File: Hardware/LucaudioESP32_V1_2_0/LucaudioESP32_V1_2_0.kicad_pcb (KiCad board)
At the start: 2 copper layers, 92.4 x 70 mm, 93 parts, among them J1 Conn_01x04_Pin, J2 Conn_Coaxial_x2, J3 USB_C_Receptacle_USB2.0_16P, J4 Conn_01x04_Socket, J5 Conn_01x05_Socket, J6 Conn_01x05_Pin, J8 USB_B_Micro, J9 AudioJack3, Q1 BC847, Q2 BC847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

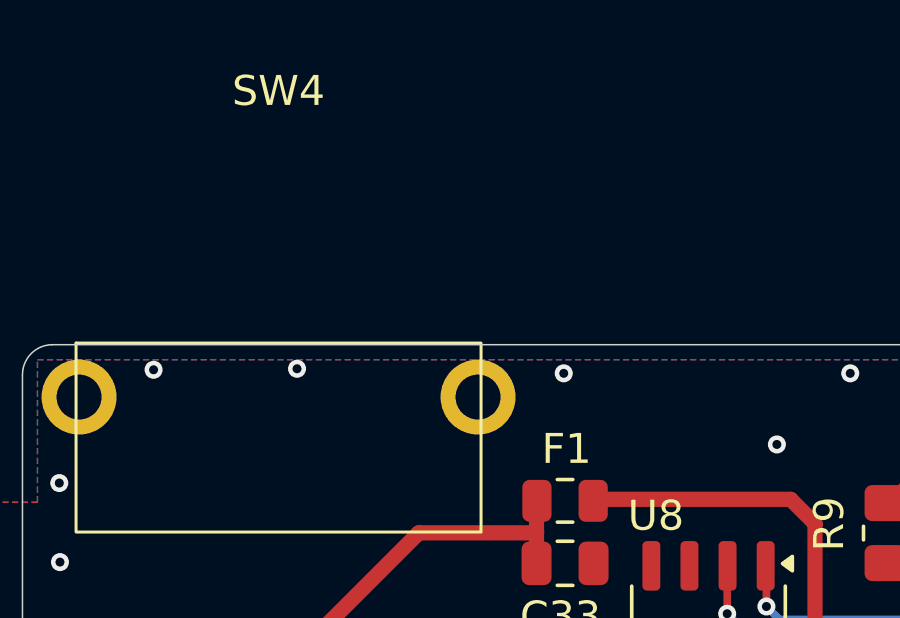
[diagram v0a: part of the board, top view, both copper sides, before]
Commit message: Revamping folders and added 2.0 and 2.1 on git
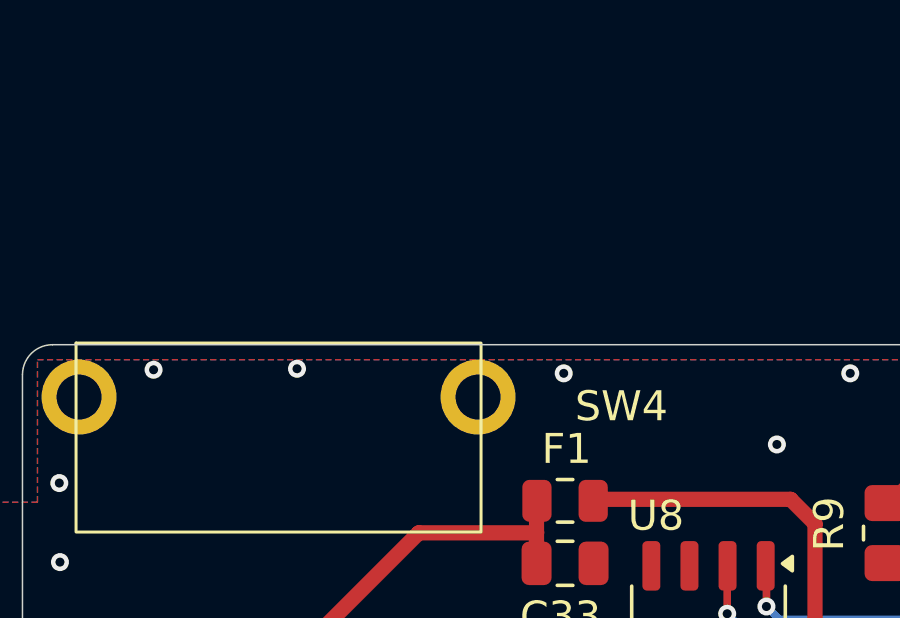
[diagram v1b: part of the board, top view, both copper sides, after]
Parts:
- Q1, Q2: value BC847 -> BC857
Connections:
- Q1 pad 2: Net-(Q1-E) -> 3V3_o
- Q1 pad 3: 3V3_o -> Net-(Q1-C)
- Q2 pad 2: Net-(Q2-E) -> 3V3_o
- Q2 pad 3: 3V3_o -> Net-(Q2-C)
- R10 pad 2: Net-(Q1-E) -> Net-(Q1-C)
- R13 pad 2: Net-(Q2-E) -> Net-(Q2-C)
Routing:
- net Net-(Q2-E): track 3.58 -> 0.00 mm
- net Net-(Q2-C): track 0.00 -> 3.58 mm
- net Net-(Q1-E): track 3.45 -> 0.00 mm
- net 3V3_o: track 64.7 -> 68.2 mm
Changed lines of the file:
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@@
 	(net 77 "Net-(LED2-A)")
 	(net 78 "Net-(SW4-B)")
-	(net 79 "Net-(Q1-E)")
-	(net 80 "Net-(Q2-E)")
+	(net 79 "Net-(Q1-C)")
+	(net 80 "Net-(Q2-C)")
 	(net 81 "unconnected-(SW4-C-Pad3)")
 	(net 82 "Net-(Q1-B)")
@@
 		(tags "fuse")
 		(property "Reference" "F1"
-			(at 0.0508 -1.7272 360)
+			(at 0.0508 -1.7272 0)
 			(layer "F.SilkS")
 			(effects
@@
 		)
 		(property "Value" "300mA"
-			(at 0 1.65 360)
+			(at 0 1.65 0)
 			(layer "F.Fab")
 			(effects
@@
 		)
 		(fp_text user "${REFERENCE}"
-			(at 0 0 360)
+			(at 0 0 0)
 			(layer "F.Fab")
 			(effects
@@
 		(tags "Through hole angled pin header THT 1x04 2.54mm single row")
 		(property "Reference" "J1"
-			(at -2.6924 -0.1786 -0)
+			(at -2.6924 -0.1786 0)
 			(layer "B.SilkS")
 			(effects
@@
 		(tags "Through hole angled pin header THT 1x05 2.54mm single row")
 		(property "Reference" "J6"
-			(at -2.8448 -0.6622 -0)
+			(at -2.8448 -0.6622 0)
 			(layer "B.SilkS")
 			(effects
@@
 		(tags "capacitor")
 		(property "Reference" "C33"
-			(at -0.1524 1.778 360)
+			(at -0.1524 1.778 0)
 			(layer "F.SilkS")
 			(effects
@@
 		)
 		(property "Value" "100nF"
-			(at 0 1.68 360)
+			(at 0 1.68 0)
 			(layer "F.Fab")
 			(effects
@@
 		)
 		(fp_text user "${REFERENCE}"
-			(at 0 0 360)
+			(at 0 0 0)
 			(layer "F.Fab")
 			(effects
@@
 		(at 136.036 76.945)
 		(property "Reference" "SW4"
-			(at 0 -19.4 0)
+			(at 11.43 -8.89 0)
 			(unlocked yes)
 			(layer "F.SilkS")
@@
 		(tags "resistor handsolder")
 		(property "Reference" "R13"
-			(at -3.302 0 360)
+			(at -3.302 0 0)
 			(layer "B.SilkS")
 			(effects
@@
 		)
 		(property "Value" "470"
-			(at 0 -1.65 360)
+			(at 0 -1.65 0)
 			(layer "B.Fab")
 			(effects
@@
 			(layers "B.Cu" "B.Paste" "B.Mask")
 			(roundrect_rratio 0.2083333333)
-			(net 80 "Net-(Q2-E)")
+			(net 80 "Net-(Q2-C)")
 			(pintype "passive")
 		)
@@
 		(tags "SOT TO_SOT_SMD")
 		(property "Reference" "Q1"
-			(at 2.921 0 360)
+			(at 2.921 0 0)
 			(layer "B.SilkS")
 			(effects
@@
 			)
 		)
-		(property "Value" "BC847"
-			(at 0 -2.4 360)
+		(property "Value" "BC857"
+			(at 0 -2.4 0)
 			(layer "B.Fab")
 			(effects
@@
 			)
 		)
-		(property "Datasheet" "http://www.infineon.com/dgdl/Infineon-BC847SERIES_BC848SERIES_BC849SERIES_BC850SERIES-DS-v01_01-en.pdf?fileId=db3a304314dca389011541d4630a1657"
+		(property "Datasheet" "https://www.onsemi.com/pub/Collateral/BC860-D.pdf"
 			(at 0 0 180)
 			(unlocked yes)
@@
 			)
 		)
-		(property "Description" "0.1A Ic, 45V Vce, NPN Transistor, SOT-23"
+		(property "Description" "0.1A Ic, 45V Vce, PNP Transistor, SOT-23"
 			(at 0 0 180)
 			(unlocked yes)
@@
 		)
 		(fp_text user "${REFERENCE}"
-			(at 0 0 360)
+			(at 0 0 0)
 			(layer "B.Fab")
 			(effects
@@
 			(layers "B.Cu" "B.Paste" "B.Mask")
 			(roundrect_rratio 0.25)
-			(net 79 "Net-(Q1-E)")
+			(net 71 "3V3_o")
 			(pinfunction "E")
 			(pintype "passive")
@@
 			(layers "B.Cu" "B.Paste" "B.Mask")
 			(roundrect_rratio 0.25)
-			(net 71 "3V3_o")
+			(net 79 "Net-(Q1-C)")
 			(pinfunction "C")
 			(pintype "passive")
@@
 		(tags "resistor handsolder")
 		(property "Reference" "R10"
-			(at -3.302 0 360)
+			(at -3.302 0 0)
 			(layer "B.SilkS")
 			(effects
@@
 		)
 		(property "Value" "470"
-			(at 0 -1.65 360)
+			(at 0 -1.65 0)
 			(layer "B.Fab")
 			(effects
@@
 		)
 		(fp_text user "${REFERENCE}"
-			(at 0 0 360)
+			(at 0 0 0)
 			(layer "B.Fab")
 			(effects
@@
 			(layers "B.Cu" "B.Paste" "B.Mask")
 			(roundrect_rratio 0.2083333333)
-			(net 79 "Net-(Q1-E)")
+			(net 79 "Net-(Q1-C)")
 			(pintype "passive")
 		)
@@
 		(tags "SOT TO_SOT_SMD")
 		(property "Reference" "Q2"
-			(at 3.429 0 360)
+			(at 3.429 0 0)
 			(layer "B.SilkS")
 			(effects
@@
 			)
 		)
-		(property "Value" "BC847"
-			(at 0 -2.4 360)
+		(property "Value" "BC857"
+			(at 0 -2.4 0)
 			(layer "B.Fab")
 			(effects
@@
 			)
 		)
-		(property "Datasheet" "http://www.infineon.com/dgdl/Infineon-BC847SERIES_BC848SERIES_BC849SERIES_BC850SERIES-DS-v01_01-en.pdf?fileId=db3a304314dca389011541d4630a1657"
+		(property "Datasheet" "https://www.onsemi.com/pub/Collateral/BC860-D.pdf"
 			(at 0 0 180)
 			(unlocked yes)
@@
 			)
 		)
-		(property "Description" "0.1A Ic, 45V Vce, NPN Transistor, SOT-23"
+		(property "Description" "0.1A Ic, 45V Vce, PNP Transistor, SOT-23"
 			(at 0 0 180)
 			(unlocked yes)
@@
 			(layers "B.Cu" "B.Paste" "B.Mask")
 			(roundrect_rratio 0.25)
-			(net 80 "Net-(Q2-E)")
+			(net 71 "3V3_o")
 			(pinfunction "E")
 			(pintype "passive")
@@
 			(layers "B.Cu" "B.Paste" "B.Mask")
 			(roundrect_rratio 0.25)
-			(net 71 "3V3_o")
+			(net 80 "Net-(Q2-C)")
 			(pinfunction "C")
 			(pintype "passive")
@@
 	)
 	(segment
+		(start 88.522 92.947)
+		(end 88.522 94.233)
+		(width 0.3048)
+		(layer "B.Cu")
+		(net 71)
+	)
+	(segment
 		(start 89.681 96.122)
 		(end 89.3 95.741)
@@
 	)
 	(segment
+		(start 87.964 94.791)
+		(end 86.5845 94.791)
+		(width 0.3048)
+		(layer "B.Cu")
+		(net 71)
+	)
+	(segment
 		(start 89.3 95.741)
 		(end 88.4595 95.741)
@@
 	)
 	(segment
+		(start 88.522 94.233)
+		(end 87.964 94.791)
+		(width 0.3048)
+		(layer "B.Cu")
+		(net 71)
+	)
+	(segment
 		(start 89.681 101.456)
 		(end 88.4595 101.456)
@@
 	)
 	(segment
-		(start 88.522 92.947)
-		(end 88.522 94.233)
-		(width 0.3048)
-		(layer "B.Cu")
-		(net 79)
-	)
-	(segment
-		(start 87.964 94.791)
-		(end 86.5845 94.791)
-		(width 0.3048)
-		(layer "B.Cu")
-		(net 79)
-	)
-	(segment
-		(start 88.522 94.233)
-		(end 87.964 94.791)
-		(width 0.3048)
-		(layer "B.Cu")
-		(net 79)
-	)
-	(segment
